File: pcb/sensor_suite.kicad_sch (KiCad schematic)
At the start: 0 parts

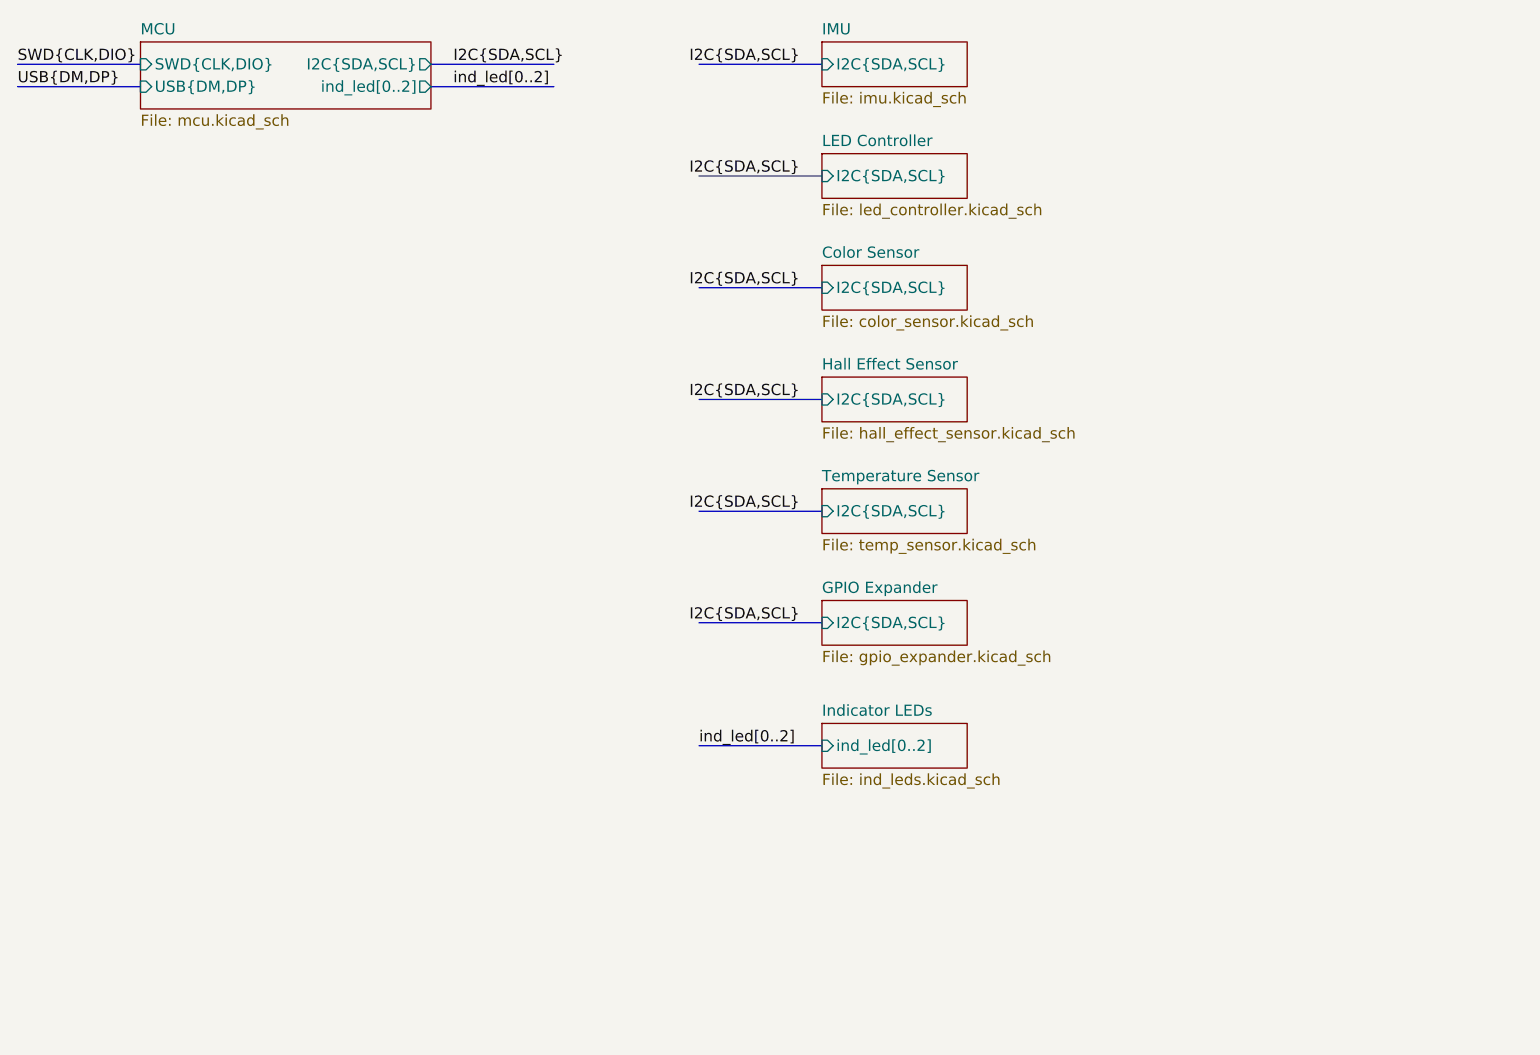
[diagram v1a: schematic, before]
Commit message: Adding some docs
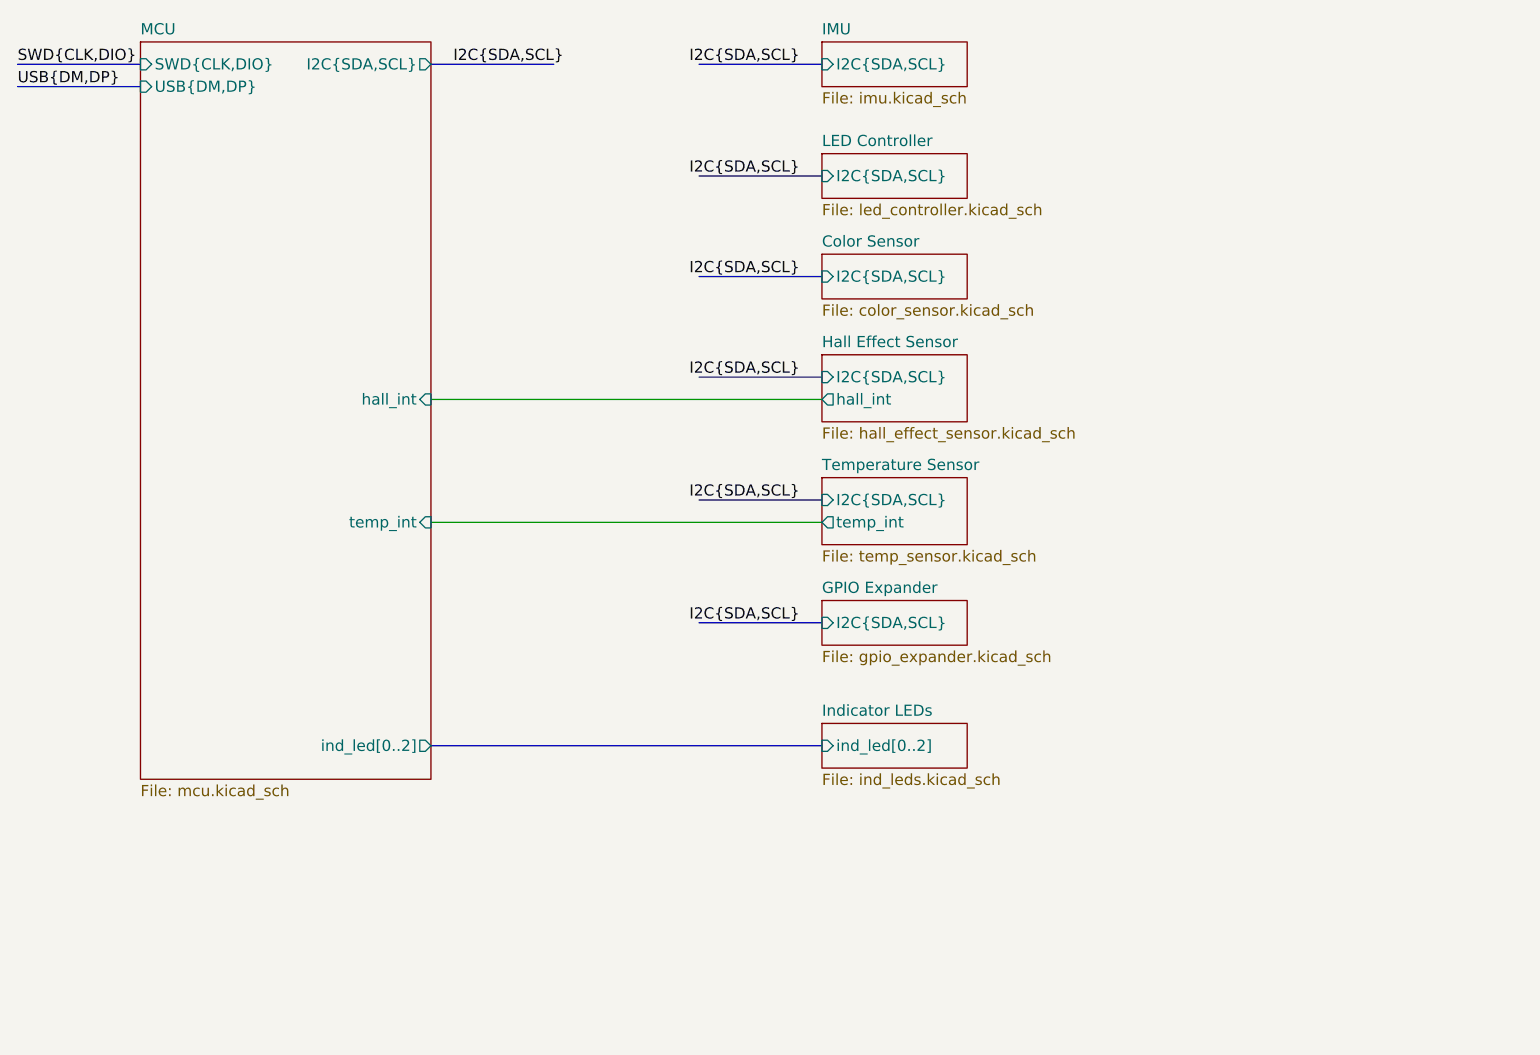
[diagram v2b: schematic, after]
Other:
- sheet Hall Effect Sensor ports: added hall_int; removed none
- sheet MCU ports: added hall_int, temp_int; removed none
- sheet Temperature Sensor ports: added temp_int; removed none
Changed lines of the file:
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@@
+		)
+	)
+	(wire
+		(pts
+			(xy 121.92 86.36) (xy 77.47 86.36)
+		)
+		(stroke
+			(width 0)
+			(type default)
 		)
 	)
@@
 	(bus
 		(pts
-			(xy 107.95 111.76) (xy 121.92 111.76)
-		)
-		(stroke
-			(width 0)
-			(type default)
-		)
-	)
-	(bus
-		(pts
-			(xy 77.47 36.83) (xy 91.44 36.83)
-		)
-		(stroke
-			(width 0)
-			(type default)
-		)
-	)
-	(bus
-		(pts
-			(xy 121.92 72.39) (xy 107.95 72.39)
-		)
-		(stroke
-			(width 0)
-			(type default)
-		)
-	)
-	(bus
-		(pts
-			(xy 121.92 85.09) (xy 107.95 85.09)
+			(xy 121.92 69.85) (xy 107.95 69.85)
+		)
+		(stroke
+			(width 0)
+			(type default)
+		)
+	)
+	(bus
+		(pts
+			(xy 121.92 83.82) (xy 107.95 83.82)
 		)
 		(stroke
@@
 	(bus
 		(pts
+			(xy 77.47 111.76) (xy 121.92 111.76)
+		)
+		(stroke
+			(width 0)
+			(type default)
+		)
+	)
+	(bus
+		(pts
 			(xy 121.92 46.99) (xy 107.95 46.99)
 		)
@@
 		)
 	)
-	(bus
-		(pts
-			(xy 121.92 59.69) (xy 107.95 59.69)
+	(wire
+		(pts
+			(xy 121.92 72.39) (xy 77.47 72.39)
+		)
+		(stroke
+			(width 0)
+			(type default)
+		)
+	)
+	(bus
+		(pts
+			(xy 121.92 58.42) (xy 107.95 58.42)
 		)
 		(stroke
@@
 	)
 	(label "I2C{SDA,SCL}"
-		(at 119.38 72.39 180)
+		(at 119.38 69.85 180)
 		(effects
 			(font
@@
 		)
 	)
-	(label "ind_led[0..2]"
-		(at 80.01 36.83 0)
-		(effects
-			(font
-				(size 1.27 1.27)
-			)
-			(justify left bottom)
-		)
-	)
 	(label "I2C{SDA,SCL}"
 		(at 119.38 34.29 180)
@@
 	)
 	(label "I2C{SDA,SCL}"
-		(at 119.38 85.09 180)
+		(at 119.38 83.82 180)
 		(effects
 			(font
@@
 	)
 	(label "I2C{SDA,SCL}"
-		(at 119.38 59.69 180)
+		(at 119.38 58.42 180)
 		(effects
 			(font
@@
 			)
 			(justify right bottom)
-		)
-	)
-	(label "ind_led[0..2]"
-		(at 107.95 111.76 0)
-		(effects
-			(font
-				(size 1.27 1.27)
-			)
-			(justify left bottom)
 		)
 	)
@@
 	(sheet
 		(at 44.45 31.75)
-		(size 33.02 7.62)
+		(size 33.02 83.82)
 		(exclude_from_sim no)
 		(in_bom yes)
@@
 		)
 		(property "Sheetfile" "mcu.kicad_sch"
-			(at 44.45 39.9546 0)
+			(at 44.45 116.1546 0)
 			(show_name no)
 			(do_not_autoplace no)
@@
 		)
 		(pin "ind_led[0..2]" output
-			(at 77.47 36.83 0)
+			(at 77.47 111.76 0)
+			(effects
+				(font
+					(size 1.27 1.27)
+				)
+				(justify right)
+			)
+		)
+		(pin "hall_int" input
+			(at 77.47 72.39 0)
+			(effects
+				(font
+					(size 1.27 1.27)
+				)
+				(justify right)
+			)
+		)
+		(pin "temp_int" input
+			(at 77.47 86.36 0)
 			(effects
 				(font
@@
 	)
 	(sheet
-		(at 121.92 69.85)
-		(size 16.51 5.08)
+		(at 121.92 67.31)
+		(size 16.51 7.62)
 		(exclude_from_sim no)
 		(in_bom yes)
@@
 		)
 		(property "Sheetname" "Hall Effect Sensor"
-			(at 121.92 69.1384 0)
+			(at 121.92 66.5984 0)
 			(show_name no)
 			(do_not_autoplace no)
@@
 		)
 		(pin "I2C{SDA,SCL}" input
+			(at 121.92 69.85 180)
+			(effects
+				(font
+					(size 1.27 1.27)
+				)
+				(justify left)
+			)
+		)
+		(pin "hall_int" output
 			(at 121.92 72.39 180)
 			(effects
@@
 	)
 	(sheet
-		(at 121.92 57.15)
+		(at 121.92 55.88)
 		(size 16.51 5.08)
 		(exclude_from_sim no)
@@
 		)
 		(property "Sheetname" "Color Sensor"
-			(at 121.92 56.4384 0)
+			(at 121.92 55.1684 0)
 			(show_name no)
 			(do_not_autoplace no)
@@
 		)
 		(property "Sheetfile" "color_sensor.kicad_sch"
-			(at 121.92 62.8146 0)
+			(at 121.92 61.5446 0)
 			(show_name no)
 			(do_not_autoplace no)
@@
 		)
 		(pin "I2C{SDA,SCL}" input
-			(at 121.92 59.69 180)
+			(at 121.92 58.42 180)
 			(effects
 				(font
@@
 	)
 	(sheet
-		(at 121.92 82.55)
-		(size 16.51 5.08)
+		(at 121.92 81.28)
+		(size 16.51 7.62)
 		(exclude_from_sim no)
 		(in_bom yes)
@@
 		)
 		(property "Sheetname" "Temperature Sensor"
-			(at 121.92 81.8384 0)
+			(at 121.92 80.5684 0)
 			(show_name no)
 			(do_not_autoplace no)
@@
 		)
 		(property "Sheetfile" "temp_sensor.kicad_sch"
-			(at 121.92 88.2146 0)
+			(at 121.92 89.4846 0)
 			(show_name no)
 			(do_not_autoplace no)
@@
 		)
 		(pin "I2C{SDA,SCL}" input
-			(at 121.92 85.09 180)
-			(effects
-				(font
+			(at 121.92 83.82 180)
+			(effects
+				(font
+					(size 1.27 1.27)
+				)
+				(justify left)
+			)
+		)
+		(pin "temp_int" output
+			(at 121.92 86.36 180)
+			(effects
+				(font

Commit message: Adding docs for GPIO and Color and removing INT
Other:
- sheet Hall Effect Sensor ports: added none; removed hall_int
- sheet MCU ports: added none; removed hall_int, temp_int
- sheet Temperature Sensor ports: added none; removed temp_int
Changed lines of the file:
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@@
 	(title_block
 		(title "Sensor Suite")
-		(date "2026-10-27")
+		(date "2026-10-28")
+		(rev "2")
 	)
 	(bus
@@
 		)
 	)
-	(wire
-		(pts
-			(xy 121.92 86.36) (xy 77.47 86.36)
-		)
-		(stroke
-			(width 0)
-			(type default)
-		)
-	)
 	(bus
 		(pts
@@
 		(pts
 			(xy 121.92 46.99) (xy 107.95 46.99)
-		)
-		(stroke
-			(width 0)
-			(type default)
-		)
-	)
-	(wire
-		(pts
-			(xy 121.92 72.39) (xy 77.47 72.39)
 		)
 		(stroke
@@
 			)
 		)
-		(pin "hall_int" input
-			(at 77.47 72.39 0)
-			(effects
-				(font
-					(size 1.27 1.27)
-				)
-				(justify right)
-			)
-		)
-		(pin "temp_int" input
-			(at 77.47 86.36 0)
-			(effects
-				(font
-					(size 1.27 1.27)
-				)
-				(justify right)
-			)
-		)
 		(instances
 			(project "sensor_suite"
@@
 	(sheet
 		(at 121.92 67.31)
-		(size 16.51 7.62)
+		(size 16.51 5.08)
 		(exclude_from_sim no)
 		(in_bom yes)
@@
 		)
 		(property "Sheetfile" "hall_effect_sensor.kicad_sch"
-			(at 121.92 75.5146 0)
+			(at 121.92 72.9746 0)
 			(show_name no)
 			(do_not_autoplace no)
@@
 		(pin "I2C{SDA,SCL}" input
 			(at 121.92 69.85 180)
-			(effects
-				(font
-					(size 1.27 1.27)
-				)
-				(justify left)
-			)
-		)
-		(pin "hall_int" output
-			(at 121.92 72.39 180)
 			(effects
 				(font
@@
 	(sheet
 		(at 121.92 81.28)
-		(size 16.51 7.62)
+		(size 16.51 5.08)
 		(exclude_from_sim no)
 		(in_bom yes)
@@
 		)
 		(property "Sheetfile" "temp_sensor.kicad_sch"
-			(at 121.92 89.4846 0)
+			(at 121.92 86.9446 0)
 			(show_name no)
 			(do_not_autoplace no)
@@
 			(effects
 				(font
-					(size 1.27 1.27)
-				)
-				(justify left)
-			)
-		)
-		(pin "temp_int" output
-			(at 121.92 86.36 180)
-			(effects
-				(font

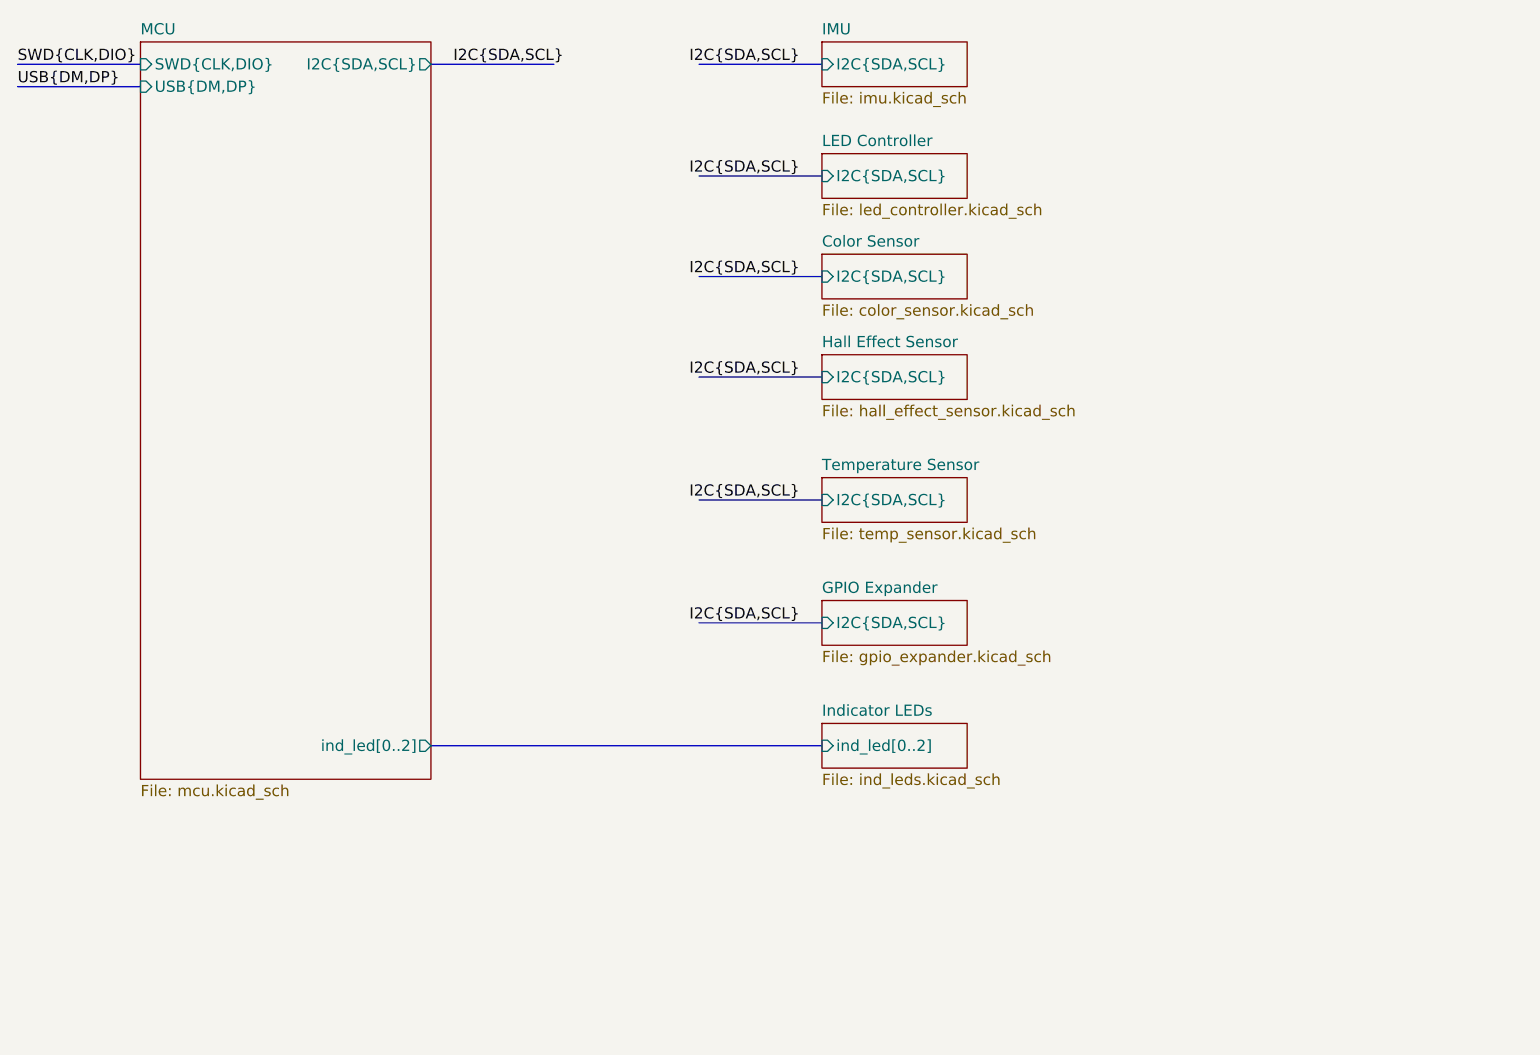
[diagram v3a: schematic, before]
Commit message: separate peripherals onto different i2c busses
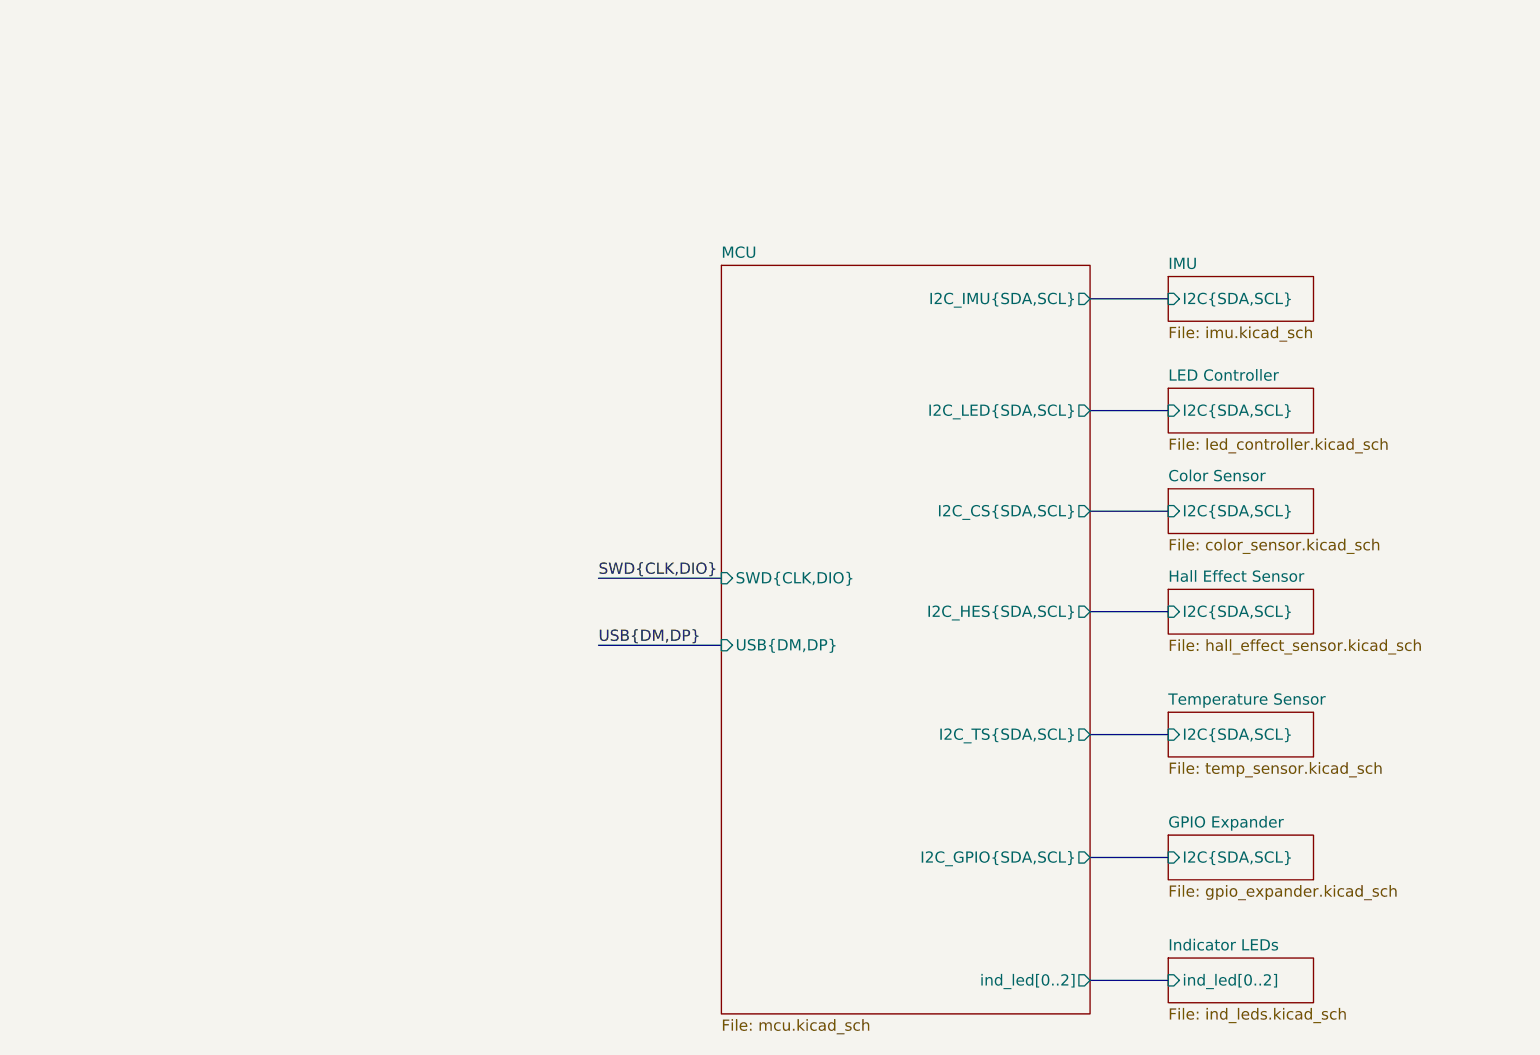
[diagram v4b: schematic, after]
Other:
- sheet MCU ports: added I2C_CS{SDA,SCL}, I2C_GPIO{SDA,SCL}, I2C_HES{SDA,SCL}, I2C_IMU{SDA,SCL}, I2C_LED{SDA,SCL}, I2C_TS{SDA,SCL}; removed I2C{SDA,SCL}
